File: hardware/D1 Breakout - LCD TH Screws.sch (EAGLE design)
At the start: 8 parts, among them J1 RJ11-4L-B

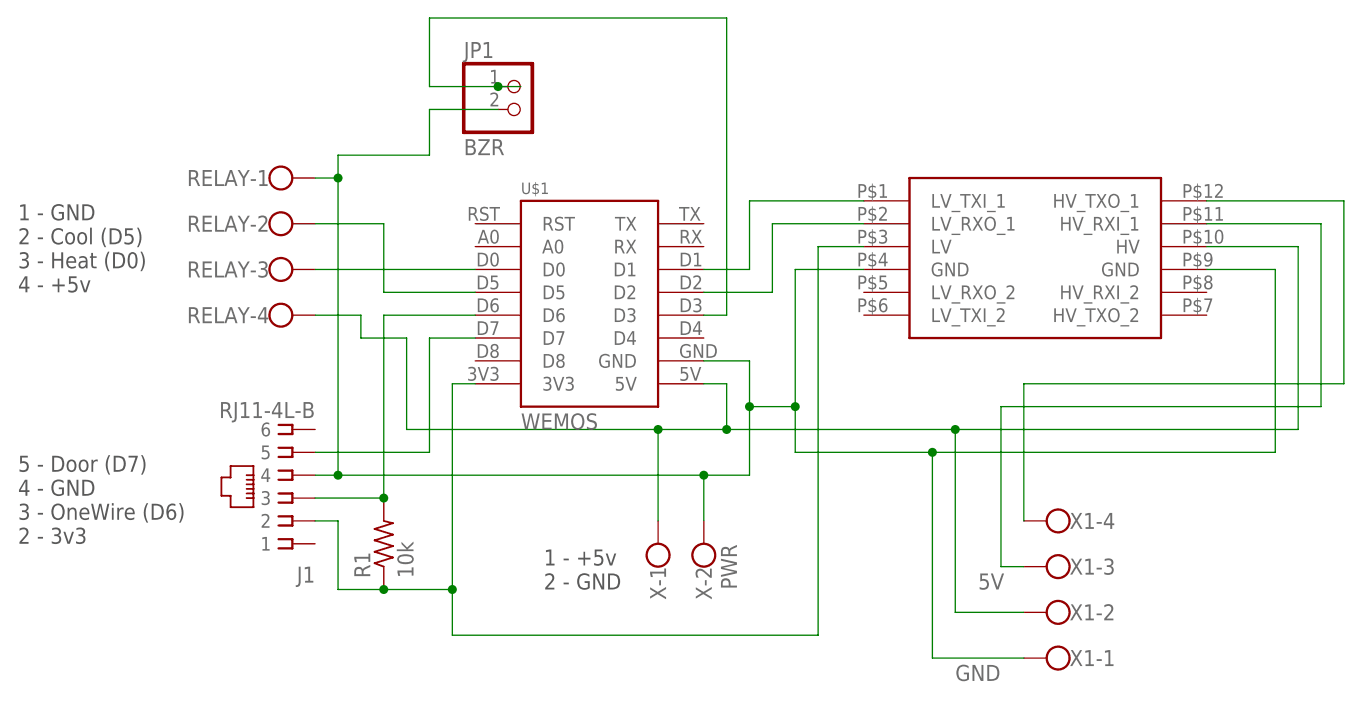
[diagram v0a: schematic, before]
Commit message: Change level shifter to most recent version
- move from https://www.sparkfun.com/products/retired/8745
  to https://www.sparkfun.com/products/12009
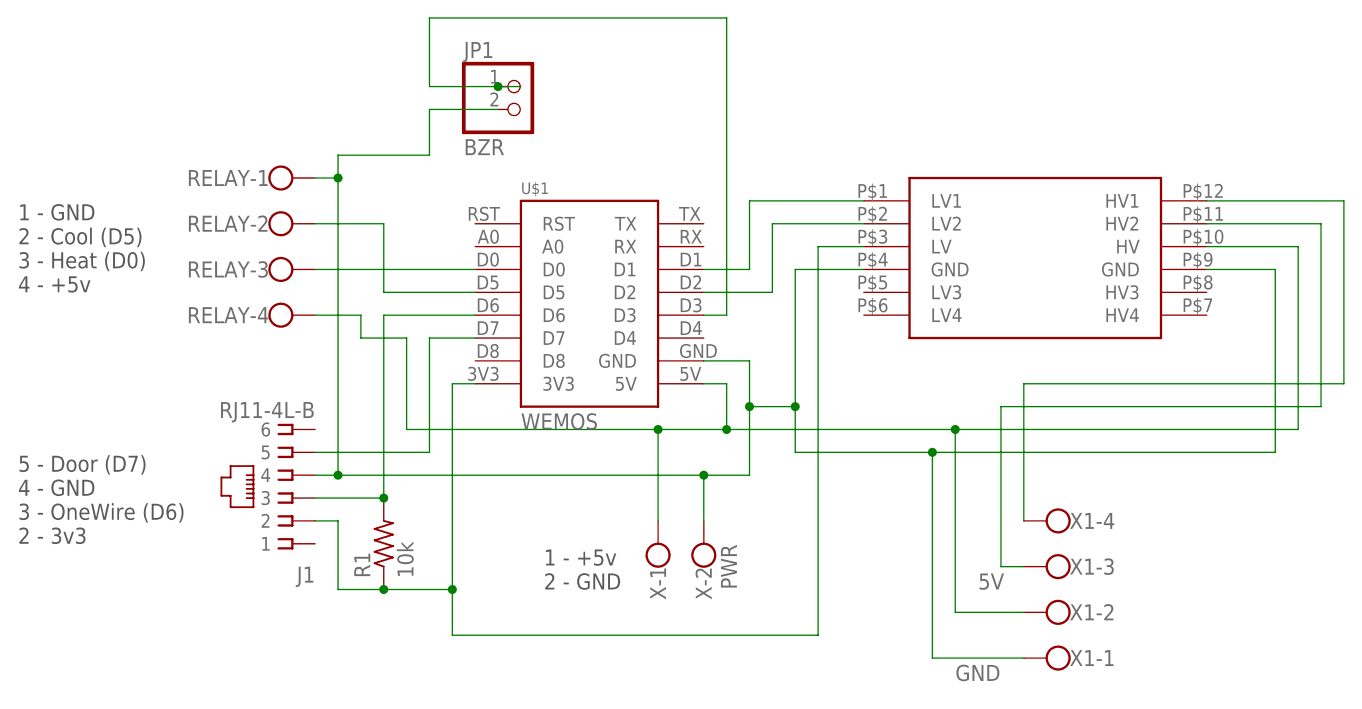
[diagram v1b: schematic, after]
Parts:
- U$3: value LOGIC_LEVEL_CONVERTER -> SPARKFUN-BOARDS_LOGIC_LEVEL_CONVERTER; device SparkFun-Boards:LOGIC_LEVEL_CONVERTER -> D1 Breakout - LCD TH Screws:SPARKFUN-BOARDS_LOGIC_LEVEL_CONVERTER
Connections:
- net N$1: now also U$3.LV1; no longer U$3.LV_TXI_1
- net N$2: now also U$3.LV2; no longer U$3.LV_RXO_1
- net N$4: now also U$3.HV1; no longer U$3.HV_TXO_1
- net N$5: now also U$3.HV2; no longer U$3.HV_RXI_1
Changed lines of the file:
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@@
 <?xml version="1.0" encoding="utf-8"?>
 <!DOCTYPE eagle SYSTEM "eagle.dtd">
-<eagle version="7.3.0">
+<eagle version="7.7.0">
 <drawing>
 <settings>
@@
 <layer number="59" name="tCarbon" color="7" fill="1" visible="no" active="no"/>
 <layer number="60" name="bCarbon" color="7" fill="1" visible="no" active="no"/>
+<layer number="88" name="SimResults" color="9" fill="1" visible="yes" active="yes"/>
+<layer number="89" name="SimProbes" color="9" fill="1" visible="yes" active="yes"/>
 <layer number="90" name="Modules" color="5" fill="1" visible="yes" active="yes"/>
 <layer number="91" name="Nets" color="2" fill="1" visible="yes" active="yes"/>
@@
 <part name="R1" library="rcl" deviceset="R-US_" device="0207/5V" value="10k"/>
 <part name="RELAY" library="con-wago-500" deviceset="W237-4" device=""/>
-<part name="U$3" library="SparkFun-Boards" deviceset="LOGIC_LEVEL_CONVERTER" device=""/>
+<part name="U$3" library="D1 Breakout - LCD TH Screws" deviceset="SPARKFUN-BOARDS_LOGIC_LEVEL_CONVERTER" device=""/>
 <part name="X1" library="con-wago-500" deviceset="W237-4" device=""/>
 <part name="JP1" library="pinhead" deviceset="PINHD-1X2" device="" value="BZR"/>
@@
 </plain>
 <instances>
-<instance part="U$1" gate="G$1" x="48.26" y="50.8"/>
-<instance part="X" gate="-1" x="63.5" y="33.02" rot="R90"/>
-<instance part="X" gate="-2" x="68.58" y="33.02" rot="R90"/>
-<instance part="J1" gate="G$1" x="22.86" y="40.64" rot="R180"/>
-<instance part="R1" gate="G$1" x="33.02" y="35.56" rot="R90"/>
-<instance part="RELAY" gate="-1" x="20.32" y="76.2"/>
-<instance part="RELAY" gate="-2" x="20.32" y="71.12"/>
-<instance part="RELAY" gate="-3" x="20.32" y="66.04"/>
-<instance part="RELAY" gate="-4" x="20.32" y="60.96"/>
-<instance part="U$3" gate="G$1" x="116.84" y="43.18"/>
-<instance part="X1" gate="-1" x="109.22" y="22.86" rot="R180"/>
-<instance part="X1" gate="-2" x="109.22" y="27.94" rot="R180"/>
-<instance part="X1" gate="-3" x="109.22" y="33.02" rot="R180"/>
-<instance part="X1" gate="-4" x="109.22" y="38.1" rot="R180"/>
-<instance part="JP1" gate="G$1" x="48.26" y="83.82"/>
+<instance part="U$1" gate="G$1" x="48.26" y="50.8" smashed="yes">
+<attribute name="NAME" x="48.26" y="74.422" size="1.27" layer="95"/>
+<attribute name="VALUE" x="48.26" y="48.26" size="1.778" layer="96"/>
+</instance>
+<instance part="X" gate="-1" x="63.5" y="33.02" smashed="yes" rot="R90">
+<attribute name="NAME" x="62.611" y="33.02" size="1.778" layer="95" rot="R270"/>
+</instance>
+<instance part="X" gate="-2" x="68.58" y="33.02" smashed="yes" rot="R90">
+<attribute name="VALUE" x="72.263" y="30.48" size="1.778" layer="96" rot="R90"/>
+<attribute name="NAME" x="67.691" y="33.02" size="1.778" layer="95" rot="R270"/>
+</instance>
+<instance part="J1" gate="G$1" x="22.86" y="40.64" smashed="yes" rot="R180">
+<attribute name="NAME" x="25.4" y="33.02" size="1.778" layer="95" rot="R180"/>
+<attribute name="VALUE" x="25.4" y="51.308" size="1.778" layer="96" rot="R180"/>
+</instance>
+<instance part="R1" gate="G$1" x="33.02" y="35.56" smashed="yes" rot="R90">
+<attribute name="NAME" x="31.5214" y="31.75" size="1.778" layer="95" rot="R90"/>
+<attribute name="VALUE" x="36.322" y="31.75" size="1.778" layer="96" rot="R90"/>
+</instance>
+<instance part="RELAY" gate="-1" x="20.32" y="76.2" smashed="yes">
+<attribute name="NAME" x="20.32" y="77.089" size="1.778" layer="95" rot="R180"/>
+</instance>
+<instance part="RELAY" gate="-2" x="20.32" y="71.12" smashed="yes">
+<attribute name="NAME" x="20.32" y="72.009" size="1.778" layer="95" rot="R180"/>
+</instance>
+<instance part="RELAY" gate="-3" x="20.32" y="66.04" smashed="yes">
+<attribute name="NAME" x="20.32" y="66.929" size="1.778" layer="95" rot="R180"/>
+</instance>
+<instance part="RELAY" gate="-4" x="20.32" y="60.96" smashed="yes">
+<attribute name="VALUE" x="17.78" y="57.277" size="1.778" layer="96"/>
+<attribute name="NAME" x="20.32" y="61.849" size="1.778" layer="95" rot="R180"/>
+</instance>
+<instance part="U$3" gate="G$1" x="116.84" y="43.18" smashed="yes"/>
+<instance part="X1" gate="-1" x="109.22" y="22.86" smashed="yes" rot="R180">
+<attribute name="NAME" x="109.22" y="21.971" size="1.778" layer="95"/>
+</instance>
+<instance part="X1" gate="-2" x="109.22" y="27.94" smashed="yes" rot="R180">
+<attribute name="NAME" x="109.22" y="27.051" size="1.778" layer="95"/>
+</instance>
+<instance part="X1" gate="-3" x="109.22" y="33.02" smashed="yes" rot="R180">
+<attribute name="NAME" x="109.22" y="32.131" size="1.778" layer="95"/>
+</instance>
+<instance part="X1" gate="-4" x="109.22" y="38.1" smashed="yes" rot="R180">
+<attribute name="VALUE" x="111.76" y="41.783" size="1.778" layer="96" rot="R180"/>
+<attribute name="NAME" x="109.22" y="37.211" size="1.778" layer="95"/>
+</instance>
+<instance part="JP1" gate="G$1" x="48.26" y="83.82" smashed="yes">
+<attribute name="NAME" x="41.91" y="89.535" size="1.778" layer="95"/>
+<attribute name="VALUE" x="41.91" y="78.74" size="1.778" layer="96"/>
+</instance>
 </instances>
 <busses>
@@
 <wire x1="68.58" y1="66.04" x2="73.66" y2="66.04" width="0.1524" layer="91"/>
 <wire x1="73.66" y1="66.04" x2="73.66" y2="73.66" width="0.1524" layer="91"/>
-<pinref part="U$3" gate="G$1" pin="LV_TXI_1"/>
+<pinref part="U$3" gate="G$1" pin="LV1"/>
 <wire x1="73.66" y1="73.66" x2="86.36" y2="73.66" width="0.1524" layer="91"/>
 </segment>
@@
 <wire x1="68.58" y1="63.5" x2="76.2" y2="63.5" width="0.1524" layer="91"/>
 <wire x1="76.2" y1="63.5" x2="76.2" y2="71.12" width="0.1524" layer="91"/>
-<pinref part="U$3" gate="G$1" pin="LV_RXO_1"/>
+<pinref part="U$3" gate="G$1" pin="LV2"/>
 <wire x1="76.2" y1="71.12" x2="86.36" y2="71.12" width="0.1524" layer="91"/>
 </segment>
@@
 <wire x1="104.14" y1="53.34" x2="139.7" y2="53.34" width="0.1524" layer="91"/>
 <wire x1="139.7" y1="53.34" x2="139.7" y2="73.66" width="0.1524" layer="91"/>
-<pinref part="U$3" gate="G$1" pin="HV_TXO_1"/>
+<pinref part="U$3" gate="G$1" pin="HV1"/>
 <wire x1="139.7" y1="73.66" x2="124.46" y2="73.66" width="0.1524" layer="91"/>
 </segment>
@@
 <wire x1="101.6" y1="50.8" x2="137.16" y2="50.8" width="0.1524" layer="91"/>
 <wire x1="137.16" y1="50.8" x2="137.16" y2="71.12" width="0.1524" layer="91"/>
-<pinref part="U$3" gate="G$1" pin="HV_RXI_1"/>
+<pinref part="U$3" gate="G$1" pin="HV2"/>
 <wire x1="137.16" y1="71.12" x2="124.46" y2="71.12" width="0.1524" layer="91"/>
 </segment>
